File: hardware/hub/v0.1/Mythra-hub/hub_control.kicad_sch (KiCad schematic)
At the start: 29 parts, among them U1 TUSB8042A, U3 BD95861MUV, Y1 24MHz

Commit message: Added power delivery control to the DFPs
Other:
- note added: "TODO: 3.3V supply"
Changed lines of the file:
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@@
     (stroke (width 0) (type solid) (color 0 0 0 0))
+  )
+  (text "TODO: 3.3V supply" (at 38.1 38.1 0)
+    (effects (font (size 1.27 1.27)) (justify left bottom))
   )
   (text "ΔVout = 504.6296mA/\n    (8*22uF*600kHz)+\n    10mohm*504.6296mA+8pH*\n    504.6296mA/166.4166ns\n      = 9.849244mV"

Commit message: Version controlled the changes from the last stream, including the addition of the 3.3V DC-DC, config I2C EEPROM and test points
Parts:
- added C77: 22uF, rhais_rcl:C1206, symbol Device:C_Small
- added C78: 470pF, rhais_rcl:C0402, symbol Device:C_Small
- added C79: 10nF, rhais_rcl:C0402, symbol Device:C_Small
- added C80: 2.2uF, rhais_rcl:C0402, symbol Device:C_Small
- added C81, C83, C84: 0.1uF, rhais_rcl:C0402, symbol Device:C_Small
- added C82: 22uF, rhais_rcl:C0603, symbol Device:C_Small
- added J12: Config I²C, rhais_connector-pinheader:PinHeader_1x05_P1.27mm_Vertical, symbol Connector_Generic:Conn_01x05
- added L6: 22uH, rhais_bourns:SRN5040, symbol Device:L_Small
- added R46, R51, R52: 10k, rhais_rcl:R0402, symbol Device:R_Small
- added R47: 14k, rhais_rcl:R0402, symbol Device:R_Small
- added R48: 6k81, rhais_rcl:R0402, symbol Device:R_Small
- added R49: 150k, rhais_rcl:R0402, symbol Device:R_Small
- added R50: 45k, rhais_rcl:R0402, symbol Device:R_Small
- added R53, R54: 4k7, rhais_rcl:R0402, symbol Device:R_Small
- added U21: SiP12109, Package_DFN_QFN:QFN-16-1EP_3x3mm_P0.5mm_EP1.7x1.7mm, symbol DX-MON:SiP12109
- added U22: M34E02-FMC, rhais_package-qfn:UDFN-8-1EP_3x2mm_P0.5mm_EP1.4x1.4mm, symbol Memory_EEPROM:M24C02-FMN
- C10, C11, C12, C13, C14, C15, C16, C22, C9: MFR (none) -> Yageo; MPN (none) -> RC0402FR-0710KL; OC_LCSC (none) -> C60490; URL_LCSC (none) -> https://www.lcsc.com/product-detail/Chip-Resistor-Surface-M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
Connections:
- net +12V: now also C77.1, R47.2, U21.1 (VIN), U21.16 (VIN)
- net +3V3: now also C82.1, C83.1, C84.1, J12.1 (Pin_1), L6.2, R50.2, R52.2, R53.2, R54.2, U22.8 (VCC)
- net GND: now also C77.2, C78.2, C79.2, C80.2, C82.2, C83.2, C84.2, J12.5 (Pin_5), R46.1, R49.2, R51.2, U21.14 (PGND), U21.15 (PGND), U21.17 (PGND), U21.3 (AGND), U22.1 (E0), U22.2 (E1), U22.3 (E2), U22.4 (VSS)
- net HUB_SDA: now reaches U1.37 (SDA)
- net HUB_SDA: now also J12.2 (Pin_2), R54.1, U22.5 (SDA)
- net HUB_SCL: now reaches U1.38 (SCL)
- net HUB_SCL: now also J12.3 (Pin_3), R53.1, U22.6 (SCL)
- new net: R46.2, R47.1, U21.8 (EN)
- new net: R50.1, R51.1, U21.6 (FB)
- new net: R49.1, U21.4 (RON)
- new net: C80.1, U21.2 (VCC)
- new net: C81.1, U21.13 (BOOT)
- new net: C79.1, U21.7 (SOFTSTART)
- new net: C78.1, R48.1
- new net: R48.2, U21.5 (COMP)
- new net 3V3_SMPS_SW: C81.2, L6.1, U21.10 (LX), U21.11 (LX), U21.12 (LX)
- new net ~{HUB_WP}: J12.4 (Pin_4), R52.1, U22.7 (~{WC})
- no-connect marks 1 -> 2
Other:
- note added: "1.6mS soft start time"
- note added: "1x Hub chip - 100mA 5x switchpoint mux's - 1mA 5x USB-PD controller - 25mA 4x DACs - 20mA"
- note added: "310mA"
- note added: "D = 1.257142MHz * 218.75ns ~= 27.5%"
- note added: "Ton = 150kohm * 17.5e-12C * (1/12V) = 218.75ns"
- note added: "Vout = 0.6V * (1 + (45kohm / 10kohm)) = 3.3V"
- note added: "f(sw) = 3.3V / (150kohm * 17.5e-12C) -> MHz ~= 1.257142MHz ~= 1.25MHz"
- note removed: "TODO: 3.3V supply"

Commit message: Completed a first pass on the azonenburg schematic checklist and begun adding the per-port indicator LEDs that had been forgotten
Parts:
- added C94, C95: 0.1uF, rhais_rcl:C0402, symbol Device:C_Small
- added C96, C97: 1uF, rhais_rcl:C0402, symbol Device:C_Small
- added C98: 10uF, rhais_rcl:C0603, symbol Device:C_Small
- U21: footprint Package_DFN_QFN:QFN-16-1EP_3x3mm_P0.5mm_EP1.7x1.7mm -> rhais_package-qfn:QFN-16-1EP_3x3mm_P0.5mm_EP1.7x1.7mm
- U22: symbol Memory_EEPROM:M24C02-FMN -> DX-MON:M34E02-FMC
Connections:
- net +1V1: now also C96.1
- net +3V3: now also C94.1, C95.1, C97.1, C98.1
- net GND: now also U22.9 (VSS), C94.2, C95.2, C96.2, C97.2, C98.2
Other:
- moved on the sheet: C10, C11, C12, C13, C14, C15, C16, C17, C9

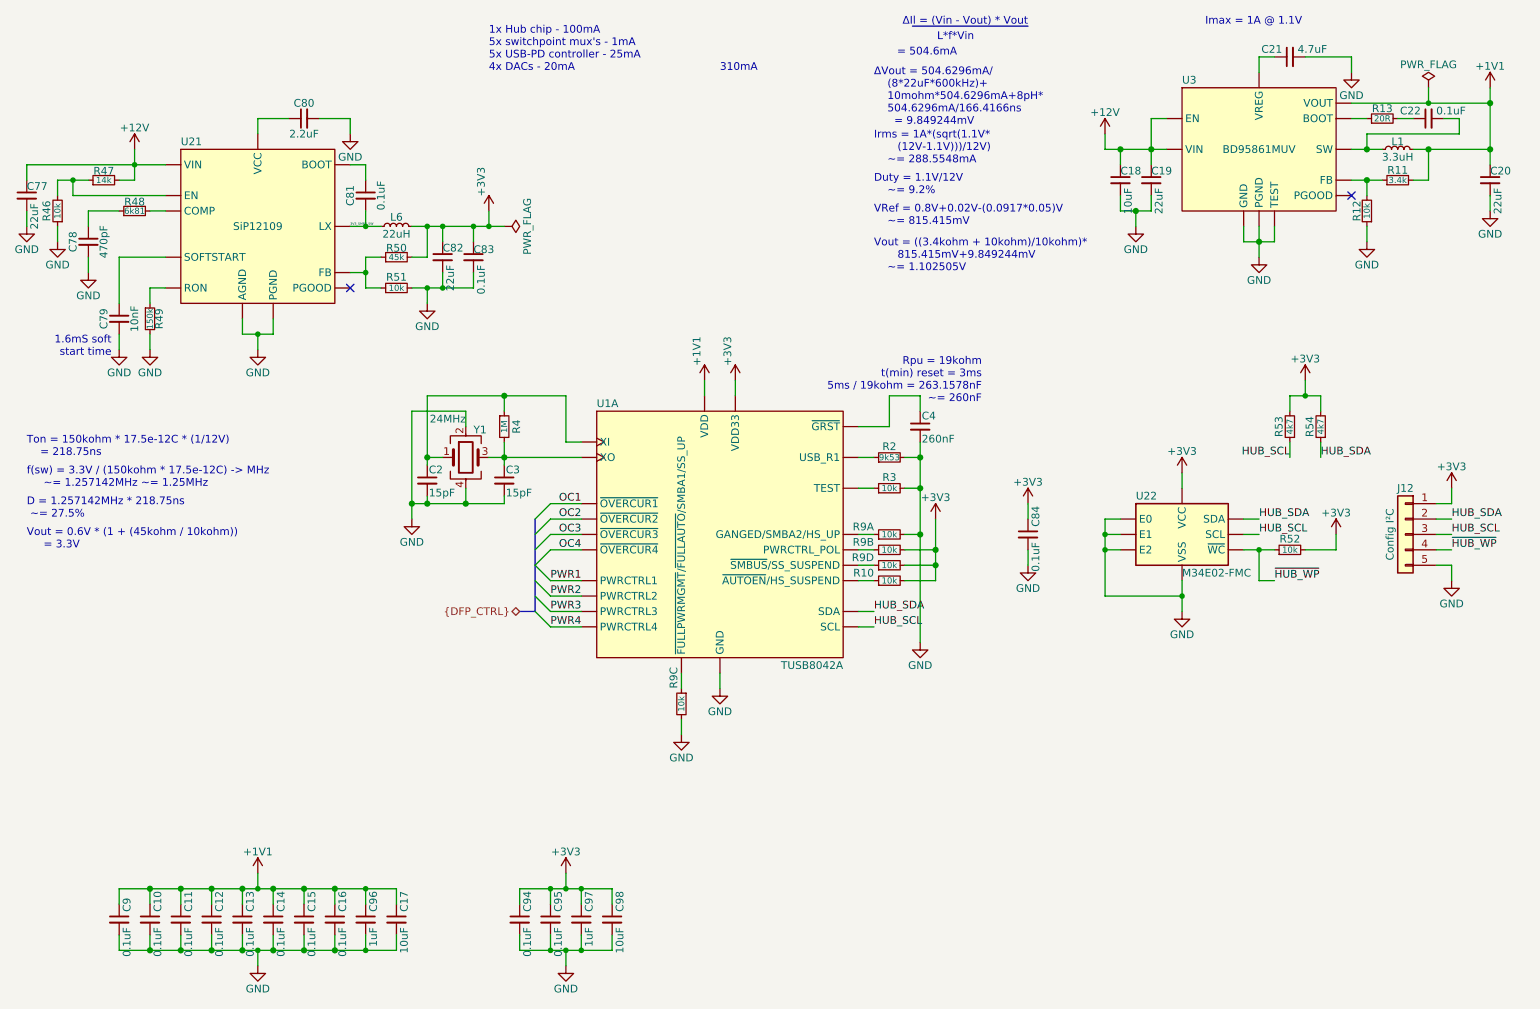
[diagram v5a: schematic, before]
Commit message: Upgraded the schematic files to KiCad 6 format and done some tidy up from the manufacturing crunch
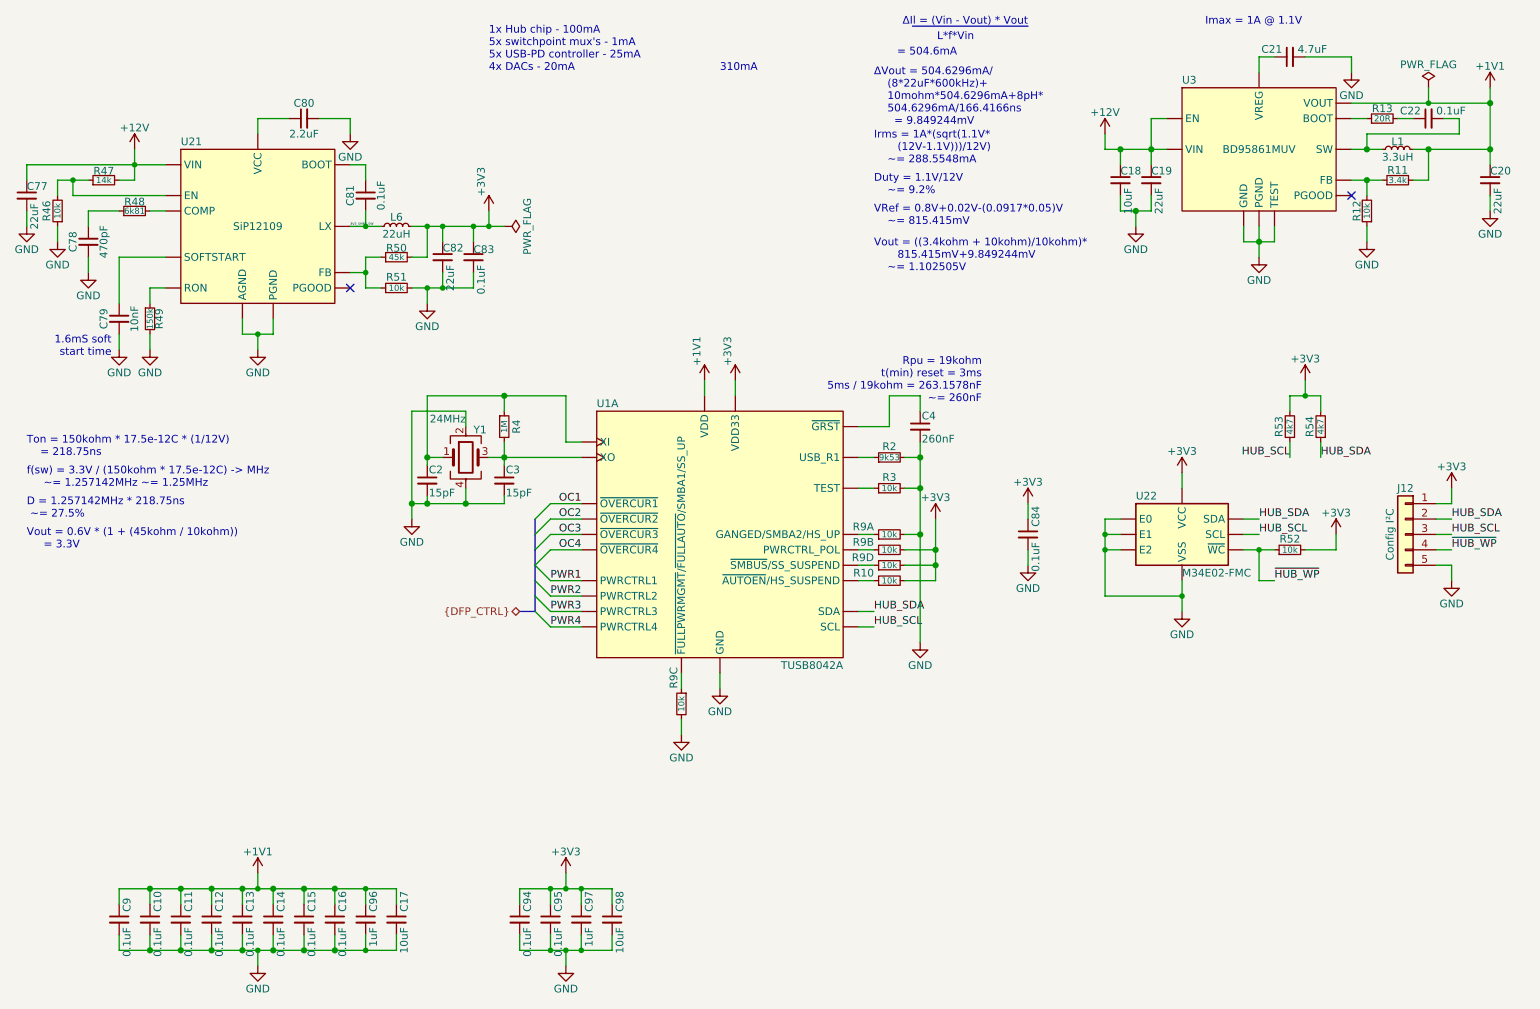
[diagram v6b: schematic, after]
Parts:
- R9: footprint pkl_dipol:R_Array_Convex_4x0402 -> rhais_rcl:R0402_Array_Convex_4; MFR (none) -> Multicomp Pro; MPN (none) -> MP005580; OC_FARNELL (none) -> 3550001; URL_FARNELL (none) -> https://uk.farnell.com/multicomp-pro/mp005580/res-n-w-isola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
